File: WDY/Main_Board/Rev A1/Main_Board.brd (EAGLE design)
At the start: 130 x 70 mm, 193 parts, among them J1 22-05-7028-02, J10 22-05-7038-03, J11 22-05-7028-02, J12 22-05-7028-02, J13 22-05-7028-02, J14 22-05-7028-02, J15 22-05-7058-05, J16 22-27-2061-06, J2 22-05-7028-02, J3 22-05-7048-04, J4 22-05-7048-04, J5 1241050-5, J6 90814-0208, J7 90814-0206, J8 90814-0208, J9 22-05-7038-03, K1 G6K-2G-Y, K2 G6K-2G-Y, K3 G6K-2G-Y, K4 G6K-2G-Y, P1 RB1-125BAG1A, SW1 B3FS-1015, SW2 B3FS-1015, T1 MMBT2222AL, U1 LPC1768FBD100, U11 SN74LVC3G17DCTR, U2 SN74LVC3G17DCTR, U3 SN74LVC3G17DCTR, U4 TPL0401A, U5 AT24C512C-SSHM-B, U6 SN74LVC2G17DBVR, U7 SN74LVC2G17DBVR, U8 LT1767EMS8E-5PBF, U9 TC1264-3.3, X1 FC-135, X2 MSTBA2

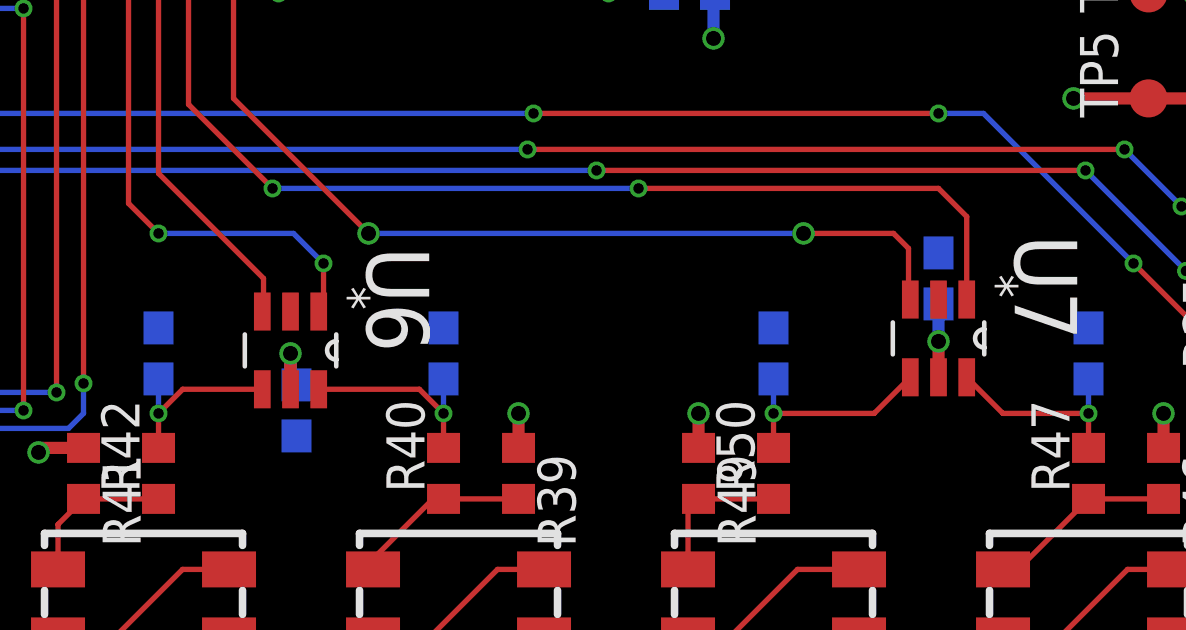
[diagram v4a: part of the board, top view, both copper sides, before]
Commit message: Fix :  Inverted input / output on all SN74LVC (U6 and U7)
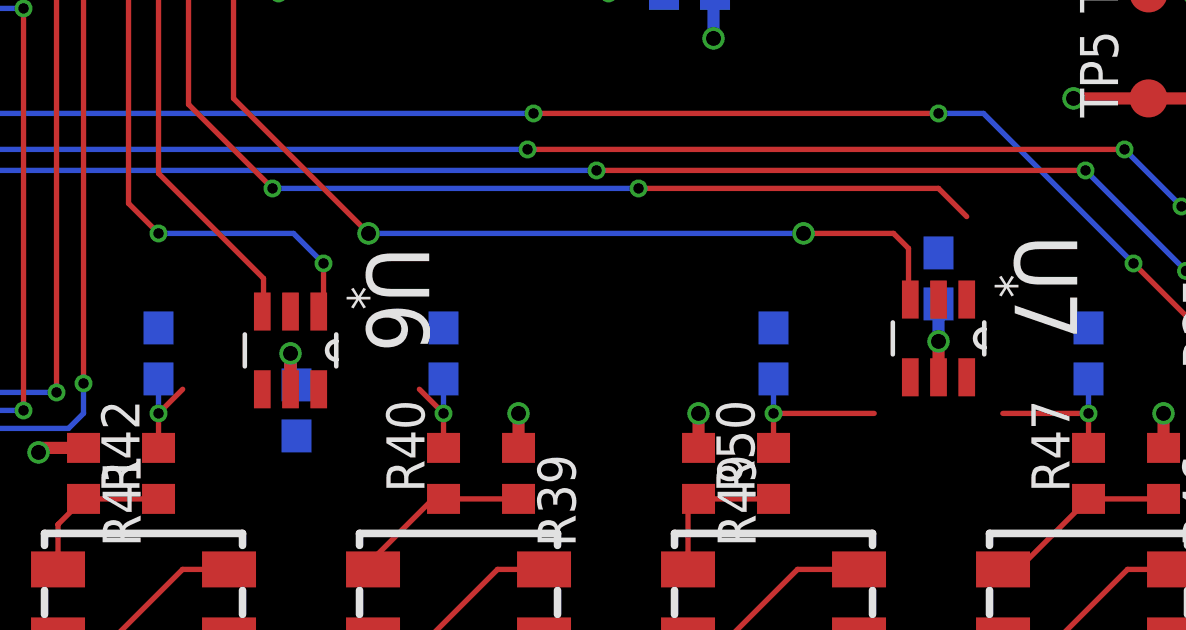
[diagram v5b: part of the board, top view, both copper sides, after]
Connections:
- net BRAKE_SENSOR_1: no longer U6.1
- net BRAKE_SENSOR_2: no longer U6.3
- net DRIVE_EN: now also U7.6; no longer U7.1
- net DRIVE_ERR: now also U7.4; no longer U7.3
- net N$38: no longer U6.4
- net N$39: no longer U6.6
- net N$41: now also U7.1; no longer U7.6
- net N$42: now also U7.3; no longer U7.4
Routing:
- net N$39: track 6.79 -> 3.44 mm
- net DRIVE_EN: track 65.2 -> 62.5 mm
- net N$38: track 6.09 -> 3.44 mm
- net N$42: track 7.36 -> 5.66 mm
- net N$41: track 6.86 -> 5.16 mm
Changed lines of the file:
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@@
 <contactref element="R42" pad="2"/>
 <contactref element="C25" pad="1"/>
-<contactref element="U6" pad="4"/>
 <wire x1="84.5" y1="22.15" x2="84.5" y2="21" width="0.1778" layer="16"/>
 <via x="84.5" y="21" extent="1-16" drill="0.35"/>
 <wire x1="84.5" y1="21" x2="84.5" y2="19.85" width="0.1778" layer="1"/>
-<wire x1="87.9602" y1="21.8046" x2="85.3046" y2="21.8046" width="0.1778" layer="1"/>
 <wire x1="85.3046" y1="21.8046" x2="84.5" y2="21" width="0.1778" layer="1"/>
 </signal>
 <signal name="N$39">
-<contactref element="U6" pad="6"/>
 <contactref element="R40" pad="2"/>
 <contactref element="C26" pad="1"/>
@@
 <via x="94" y="21" extent="1-16" drill="0.35"/>
 <wire x1="94" y1="21" x2="94" y2="19.85" width="0.1778" layer="1"/>
-<wire x1="89.8398" y1="21.8046" x2="93.1954" y2="21.8046" width="0.1778" layer="1"/>
 <wire x1="93.1954" y1="21.8046" x2="94" y2="21" width="0.1778" layer="1"/>
 </signal>
 <signal name="BRAKE_SENSOR_1">
-<contactref element="U6" pad="1"/>
 <contactref element="U1" pad="81"/>
-<wire x1="89.8398" y1="24.3954" x2="90" y2="24.5556" width="0.1778" layer="1"/>
 <wire x1="90" y1="24.5556" x2="90" y2="26" width="0.1778" layer="1"/>
 <wire x1="59.88" y1="40" x2="65" y2="40" width="0.1778" layer="1"/>
@@
 </signal>
 <signal name="BRAKE_SENSOR_2">
-<contactref element="U6" pad="3"/>
 <contactref element="U1" pad="80"/>
-<wire x1="87.9602" y1="24.3954" x2="88" y2="24.4352" width="0.1778" layer="1"/>
 <wire x1="88" y1="24.4352" x2="88" y2="25.5" width="0.1778" layer="1"/>
 <wire x1="64" y1="40.7" x2="63.8" y2="40.5" width="0.1778" layer="1"/>
@@
 </signal>
 <signal name="N$41">
-<contactref element="U7" pad="6"/>
 <contactref element="C28" pad="1"/>
 <contactref element="R47" pad="2"/>
@@
 <via x="115.5" y="21" extent="1-16" drill="0.35"/>
 <wire x1="115.5" y1="21" x2="115.5" y2="19.85" width="0.1778" layer="1"/>
-<wire x1="111.4398" y1="22.2046" x2="112.6444" y2="21" width="0.1778" layer="1"/>
 <wire x1="112.6444" y1="21" x2="115.5" y2="21" width="0.1778" layer="1"/>
+<contactref element="U7" pad="1"/>
+<wire x1="111.4398" y1="24.7954" x2="112.6444" y2="21" width="0" layer="19" extent="1-1"/>
 </signal>
 <signal name="N$42">
-<contactref element="U7" pad="4"/>
 <contactref element="C27" pad="1"/>
 <contactref element="R50" pad="2"/>
@@
 <via x="105" y="21" extent="1-16" drill="0.35"/>
 <wire x1="105" y1="21" x2="105" y2="19.85" width="0.1778" layer="1"/>
-<wire x1="109.5602" y1="22.2046" x2="108.3556" y2="21" width="0.1778" layer="1"/>
 <wire x1="108.3556" y1="21" x2="105" y2="21" width="0.1778" layer="1"/>
+<contactref element="U7" pad="3"/>
+<wire x1="108.3556" y1="21" x2="109.5602" y2="24.7954" width="0" layer="19" extent="1-1"/>
 </signal>
 <signal name="DRIVE_EN">
-<contactref element="U7" pad="1"/>
 <contactref element="U1" pad="79"/>
 <wire x1="110.5" y1="28.5" x2="100.5" y2="28.5" width="0.1778" layer="1"/>
@@
 <wire x1="85.5" y1="31.3" x2="88.3" y2="28.5" width="0.1778" layer="1"/>
 <via x="84.2" y="41.3" extent="1-16" drill="0.35"/>
-<wire x1="111.4398" y1="24.7954" x2="111.4398" y2="27.5602" width="0.1778" layer="1"/>
 <wire x1="111.4398" y1="27.5602" x2="110.5" y2="28.5" width="0.1778" layer="1"/>
+<contactref element="U7" pad="6"/>
+<wire x1="111.4398" y1="27.5602" x2="111.4398" y2="22.2046" width="0" layer="19" extent="1-1"/>
 </signal>
 <signal name="DRIVE_ERR">
-<contactref element="U7" pad="3"/>
 <contactref element="U1" pad="78"/>
 <wire x1="106" y1="27" x2="91.5" y2="27" width="0.1778" layer="16"/>
@@
 <via x="91.5" y="27" extent="1-16" drill="0.5"/>
 <via x="85.6" y="41.9" extent="1-16" drill="0.35"/>
-<wire x1="109.5602" y1="24.7954" x2="109.5" y2="24.8556" width="0.1778" layer="1"/>
 <wire x1="109.5" y1="24.8556" x2="109.5" y2="26.5" width="0.1778" layer="1"/>
 <wire x1="109.5" y1="26.5" x2="109" y2="27" width="0.1778" layer="1"/>
 <wire x1="109" y1="27" x2="106" y2="27" width="0.1778" layer="1"/>
+<contactref element="U7" pad="4"/>
+<wire x1="109.5" y1="24.8556" x2="109.5602" y2="22.2046" width="0" layer="19" extent="1-1"/>
 </signal>
 <signal name="RTCX1">

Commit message: Rotate U$15
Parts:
- moved C53 4.30 mm to (88.9, 25.4), turned to 90 degrees
- moved U$14 1.50 mm to (6.00, 53.4), flipped to the top, turned to 90 degrees
- moved JP1 1.40 mm to (1.00, 39.6)
- moved C52 0.30 mm to (110.5, 25.2)
- turned U6 to 90 degrees
- turned U7 to 90 degrees
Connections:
- net BRAKE_SENSOR_1: now also U6.6
- net BRAKE_SENSOR_2: now also U6.4
- net N$38: now also U6.3
- net N$39: now also U6.1
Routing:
- net VBAT+: track 4.83 -> 99.7 mm, vias 1 -> 2
- net AVDD: track 16.7 -> 7.73 mm
- net N$39: track 3.44 -> 11.2 mm, vias 1 -> 3
- net N$38: track 3.44 -> 9.31 mm, vias 1 -> 3
- net N$41: track 5.16 -> 10.1 mm, vias 1 -> 3
- net N$42: track 5.66 -> 10.5 mm, vias 1 -> 3
- net BRAKE_SENSOR_1: track 43.8 -> 41.1 mm, vias 4 -> 2
- net BRAKE_SENSOR_2: track 42.1 -> 44.4 mm
- net DRIVE_ERR: track 63.1 -> 65.3 mm
- net N$22: track 34.0 -> 32.6 mm
- net DRIVE_EN: track 62.5 -> 63.0 mm
- net +3V3: track 156.1 -> 156.6 mm
- removed copper zone on layer 3, net VBAT+

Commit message: Put boot and reset button on top layer
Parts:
- moved SW1 1.12 mm to (107.2, 39.0), flipped to the top, turned to 0 degrees
- moved SW2 1.12 mm to (94.5, 39.0), flipped to the top, turned to 180 degrees
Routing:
- net RESET: track 62.7 -> 69.0 mm
- net N$5: track 14.7 -> 19.6 mm, vias 0 -> 1
- net +3V3: track 156.6 -> 152.8 mm
- net JTAG_TCK: track 32.7 -> 30.2 mm
- net JTAG_TMS: track 32.6 -> 30.1 mm
- net JTAG_TDI: track 35.1 -> 33.0 mm
- net JTAG_TDO: track 37.2 -> 35.2 mm
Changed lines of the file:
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@@
 <grid distance="0.5" unitdist="mm" unit="mm" style="lines" multiple="1" display="no" altdistance="0.1" altunitdist="mm" altunit="mm"/>
 <layers>
-<layer number="1" name="Top" color="4" fill="1" visible="yes" active="yes"/>
-<layer number="2" name="Route2" color="6" fill="1" visible="yes" active="yes"/>
+<layer number="1" name="Top" color="4" fill="1" visible="no" active="yes"/>
+<layer number="2" name="Route2" color="6" fill="1" visible="no" active="yes"/>
 <layer number="3" name="Route3" color="20" fill="1" visible="no" active="yes"/>
 <layer number="14" name="Route14" color="1" fill="6" visible="no" active="no"/>
@@
 <layer number="19" name="Unrouted" color="6" fill="1" visible="yes" active="yes"/>
 <layer number="20" name="Dimension" color="15" fill="1" visible="yes" active="yes"/>
-<layer number="21" name="tPlace" color="7" fill="1" visible="yes" active="yes"/>
+<layer number="21" name="tPlace" color="7" fill="1" visible="no" active="yes"/>
 <layer number="22" name="bPlace" color="7" fill="1" visible="yes" active="yes"/>
-<layer number="23" name="tOrigins" color="15" fill="1" visible="yes" active="yes"/>
+<layer number="23" name="tOrigins" color="15" fill="1" visible="no" active="yes"/>
 <layer number="24" name="bOrigins" color="15" fill="1" visible="yes" active="yes"/>
-<layer number="25" name="tNames" color="7" fill="1" visible="yes" active="yes"/>
+<layer number="25" name="tNames" color="7" fill="1" visible="no" active="yes"/>
 <layer number="26" name="bNames" color="7" fill="1" visible="yes" active="yes"/>
-<layer number="27" name="tValues" color="7" fill="1" visible="yes" active="yes"/>
+<layer number="27" name="tValues" color="7" fill="1" visible="no" active="yes"/>
 <layer number="28" name="bValues" color="7" fill="1" visible="yes" active="yes"/>
 <layer number="29" name="tStop" color="7" fill="3" visible="no" active="yes"/>
@@
 <layer number="49" name="Reference" color="7" fill="1" visible="yes" active="yes"/>
 <layer number="50" name="dxf" color="7" fill="1" visible="yes" active="yes"/>
-<layer number="51" name="tDocu" color="7" fill="1" visible="yes" active="yes"/>
+<layer number="51" name="tDocu" color="7" fill="1" visible="no" active="yes"/>
 <layer number="52" name="bDocu" color="7" fill="1" visible="yes" active="yes"/>
 <layer number="53" name="tGND_GNDA" color="7" fill="1" visible="yes" active="yes"/>
@@
 </element>
 <element name="C55" library="rcl" package="C0603" value="0.1uF" x="74.5" y="22.3"/>
-<element name="SW1" library="Switch_SMT" package="B3FS" value="B3FS-1015" x="106.2" y="39.5" rot="MR180"/>
-<element name="SW2" library="Switch_SMT" package="B3FS" value="B3FS-1015" x="93.5" y="39.5" rot="MR0"/>
+<element name="SW1" library="Switch_SMT" package="B3FS" value="B3FS-1015" x="107.2" y="39"/>
+<element name="SW2" library="Switch_SMT" package="B3FS" value="B3FS-1015" x="94.5" y="39" rot="R180"/>
 <element name="R11" library="rcl" package="R0603" value="10K" x="102.2" y="35" rot="MR180"/>
 <element name="R67" library="rcl" package="R0603" value="10K" x="90.9" y="43.9" rot="MR180"/>
@@
 <wire x1="66.5" y1="24.36" x2="66.5" y2="23.3" width="0.4064" layer="16"/>
 <wire x1="66.5" y1="23.3" x2="66.2" y2="23" width="0.4064" layer="16"/>
-<wire x1="29" y1="32.58" x2="29" y2="36.4" width="0.4064" layer="16"/>
 <wire x1="35.5" y1="33.8" x2="34.1" y2="33.8" width="0.4064" layer="1"/>
 <wire x1="34.1" y1="33.8" x2="33.5" y2="34.4" width="0.4064" layer="1"/>
@@
 <wire x1="73.7" y1="24.425" x2="75.3" y2="24.425" width="0.4064" layer="1"/>
 <wire x1="75.3" y1="24.425" x2="75.325" y2="24.45" width="0.4064" layer="1"/>
+<wire x1="29" y1="35.35" x2="29" y2="32.58" width="0" layer="19" extent="1-16"/>
 </signal>
 <signal name="N$4">
@@
 <contactref element="U1" pad="1"/>
 <contactref element="J5" pad="9"/>
-<wire x1="29" y1="22.42" x2="30.92" y2="22.42" width="0.1778" layer="16"/>
 <wire x1="30.92" y1="22.42" x2="31.5" y2="23" width="0.1778" layer="16"/>
 <wire x1="31.5" y1="23" x2="31.5" y2="25.5" width="0.1778" layer="16"/>
 <wire x1="31.5" y1="25.5" x2="32" y2="26" width="0.1778" layer="16"/>
-<wire x1="32" y1="26" x2="45" y2="26" width="0.1778" layer="16"/>
-<wire x1="45" y1="26" x2="45.9" y2="26" width="0.1778" layer="16"/>
+<wire x1="32" y1="26" x2="45.9" y2="26" width="0.1778" layer="16"/>
 <wire x1="45.9" y1="26" x2="46" y2="26.1" width="0.1778" layer="16"/>
 <via x="46" y="26.1" extent="1-16" drill="0.35"/>
@@
 <wire x1="61.5" y1="28" x2="61.5" y2="28.88" width="0.1778" layer="1"/>
 <wire x1="46" y1="26.1" x2="47.4" y2="27.5" width="0.1778" layer="1"/>
+<wire x1="29" y1="22.42" x2="30.92" y2="22.42" width="0" layer="19" extent="16-16"/>
 </signal>
 <signal name="JTAG_TDI" class="1">
@@
 <contactref element="J5" pad="7"/>
 <wire x1="29" y1="24.96" x2="29.96" y2="24.96" width="0.1778" layer="16"/>
-<wire x1="29.96" y1="24.96" x2="31.5" y2="26.5" width="0.1778" layer="16"/>
 <wire x1="62" y1="28.88" x2="62" y2="28" width="0.1778" layer="1"/>
 <wire x1="62" y1="28" x2="61" y2="27" width="0.1778" layer="1"/>
@@
 <wire x1="36.7" y1="26.7" x2="36.5" y2="26.5" width="0.1778" layer="16"/>
 <wire x1="36.5" y1="26.5" x2="31.5" y2="26.5" width="0.1778" layer="16"/>
+<wire x1="29.96" y1="24.96" x2="31.5" y2="26.5" width="0" layer="19" extent="16-16"/>
 </signal>
 <signal name="JTAG_TMS" class="1">
@@
 <contactref element="J5" pad="10"/>
 <wire x1="34" y1="22.42" x2="34.08" y2="22.5" width="0.1778" layer="16"/>
-<wire x1="34.08" y1="22.5" x2="36.5" y2="22.5" width="0.1778" layer="16"/>
 <wire x1="36.5" y1="22.5" x2="38.9" y2="24.9" width="0.1778" layer="16"/>
 <wire x1="38.9" y1="24.9" x2="49" y2="24.9" width="0.1778" layer="16"/>
@@
 <wire x1="61.5" y1="26.5" x2="62.5" y2="27.5" width="0.1778" layer="1"/>
 <wire x1="62.5" y1="27.5" x2="62.5" y2="28.88" width="0.1778" layer="1"/>
+<wire x1="34.08" y1="22.5" x2="36.5" y2="22.5" width="0" layer="19" extent="16-16"/>
 </signal>
 <signal name="JTAG_TCK" class="1">
@@
 <contactref element="J5" pad="8"/>
 <wire x1="34" y1="24.96" x2="34.04" y2="25" width="0.1778" layer="16"/>
-<wire x1="34.04" y1="25" x2="36.5" y2="25" width="0.1778" layer="16"/>
 <wire x1="36.5" y1="25" x2="37" y2="25.5" width="0.1778" layer="16"/>
 <wire x1="37" y1="25.5" x2="47.5" y2="25.5" width="0.1778" layer="16"/>
@@
 <wire x1="63.5" y1="26.5" x2="63.5" y2="28.88" width="0.1778" layer="1"/>
 <wire x1="63.5" y1="26.5" x2="62.3" y2="25.3" width="0.1778" layer="1"/>
+<wire x1="34.04" y1="25" x2="36.5" y2="25" width="0" layer="19" extent="16-16"/>
 </signal>
 <signal name="JTAG_RST" class="1">
@@
 <via x="72.8" y="37.6" extent="1-16" drill="0.35"/>
 <via x="72.8" y="34.8" extent="1-16" drill="0.35"/>
-<wire x1="102.2" y1="37.25" x2="110.2" y2="37.25" width="0.1778" layer="16"/>
+<wire x1="103.2" y1="41.25" x2="111.2" y2="41.25" width="0.1778" layer="1"/>
 <wire x1="101.35" y1="35" x2="99.5" y2="35" width="0.1778" layer="16"/>
 <wire x1="72.8" y1="37.6" x2="85.9" y2="37.6" width="0.1778" layer="16"/>
@@
 <wire x1="88.5" y1="35" x2="99.5" y2="35" width="0.1778" layer="1"/>
 <via x="99.5" y="35" extent="1-16" drill="0.35"/>
-<wire x1="101.35" y1="35" x2="101.35" y2="35.85" width="0.1778" layer="16"/>
-<wire x1="101.35" y1="35.85" x2="102.2" y2="36.7" width="0.1778" layer="16"/>
-<wire x1="102.2" y1="36.7" x2="102.2" y2="37.25" width="0.1778" layer="16"/>
+<wire x1="103.2" y1="41.8" x2="103.2" y2="41.25" width="0.1778" layer="1"/>
+<wire x1="103.2" y1="41.25" x2="102.25" y2="41.25" width="0.1778" layer="1"/>
+<wire x1="102.25" y1="41.25" x2="101.5" y2="40.5" width="0.1778" layer="1"/>
+<wire x1="101.5" y1="40.5" x2="101.5" y2="37" width="0.1778" layer="1"/>
+<wire x1="101.5" y1="37" x2="99.5" y2="35" width="0.1778" layer="1"/>
 </signal>
 <signal name="HMI_LCD_BACKLIGHT">
@@
 <contactref element="SW2" pad="4"/>
 <contactref element="SW2" pad="3"/>
-<wire x1="89.5" y1="41.75" x2="97.5" y2="41.75" width="0.1778" layer="16"/>
+<wire x1="90.5" y1="36.75" x2="98.5" y2="36.75" width="0.1778" layer="1"/>
 <contactref element="R71" pad="2"/>
 <contactref element="R72" pad="2"/>
@@
 <wire x1="89.85" y1="46" x2="89.85" y2="44.1" width="0.1778" layer="16"/>
 <wire x1="89.85" y1="44.1" x2="90.05" y2="43.9" width="0.1778" layer="16"/>
-<wire x1="90.05" y1="43.9" x2="90.05" y2="42.3" width="0.1778" layer="16"/>
-<wire x1="90.05" y1="42.3" x2="89.5" y2="41.75" width="0.1778" layer="16"/>
+<wire x1="90.5" y1="36.75" x2="90.5" y2="39" width="0.1778" layer="1"/>
+<via x="90.5" y="39" extent="1-16" drill="0.35"/>
+<wire x1="90.5" y1="39" x2="90.05" y2="39.45" width="0.1778" layer="16"/>
+<wire x1="90.05" y1="39.45" x2="90.05" y2="43.9" width="0.1778" layer="16"/>
 </signal>
 <signal name="BOOT_SELECT_P2_12" class="1">
@@
 <via x="76" y="46" extent="1-16" drill="0.35"/>
 <wire x1="76" y1="46" x2="84.5" y2="46" width="0.1778" layer="16"/>
-<wire x1="86.6" y1="48.1" x2="88.15" y2="48.1" width="0.1778" layer="16"/>
 <wire x1="86.6" y1="48.1" x2="84.5" y2="46" width="0.1778" layer="16"/>
+<wire x1="86.6" y1="48.1" x2="88.15" y2="48.1" width="0.1778" layer="16"/>
 </signal>
 </signals>

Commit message: Put J16 on top layer
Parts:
- flipped J16 to the top
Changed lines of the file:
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@@
 <grid distance="0.5" unitdist="mm" unit="mm" style="lines" multiple="1" display="no" altdistance="0.1" altunitdist="mm" altunit="mm"/>
 <layers>
-<layer number="1" name="Top" color="4" fill="1" visible="no" active="yes"/>
-<layer number="2" name="Route2" color="6" fill="1" visible="no" active="yes"/>
+<layer number="1" name="Top" color="4" fill="1" visible="yes" active="yes"/>
+<layer number="2" name="Route2" color="6" fill="1" visible="yes" active="yes"/>
 <layer number="3" name="Route3" color="20" fill="1" visible="no" active="yes"/>
 <layer number="14" name="Route14" color="1" fill="6" visible="no" active="no"/>
@@
 <layer number="19" name="Unrouted" color="6" fill="1" visible="yes" active="yes"/>
 <layer number="20" name="Dimension" color="15" fill="1" visible="yes" active="yes"/>
-<layer number="21" name="tPlace" color="7" fill="1" visible="no" active="yes"/>
+<layer number="21" name="tPlace" color="7" fill="1" visible="yes" active="yes"/>
 <layer number="22" name="bPlace" color="7" fill="1" visible="yes" active="yes"/>
-<layer number="23" name="tOrigins" color="15" fill="1" visible="no" active="yes"/>
+<layer number="23" name="tOrigins" color="15" fill="1" visible="yes" active="yes"/>
 <layer number="24" name="bOrigins" color="15" fill="1" visible="yes" active="yes"/>
-<layer number="25" name="tNames" color="7" fill="1" visible="no" active="yes"/>
+<layer number="25" name="tNames" color="7" fill="1" visible="yes" active="yes"/>
 <layer number="26" name="bNames" color="7" fill="1" visible="yes" active="yes"/>
-<layer number="27" name="tValues" color="7" fill="1" visible="no" active="yes"/>
+<layer number="27" name="tValues" color="7" fill="1" visible="yes" active="yes"/>
 <layer number="28" name="bValues" color="7" fill="1" visible="yes" active="yes"/>
 <layer number="29" name="tStop" color="7" fill="3" visible="no" active="yes"/>
@@
 <layer number="49" name="Reference" color="7" fill="1" visible="yes" active="yes"/>
 <layer number="50" name="dxf" color="7" fill="1" visible="yes" active="yes"/>
-<layer number="51" name="tDocu" color="7" fill="1" visible="no" active="yes"/>
+<layer number="51" name="tDocu" color="7" fill="1" visible="yes" active="yes"/>
 <layer number="52" name="bDocu" color="7" fill="1" visible="yes" active="yes"/>
 <layer number="53" name="tGND_GNDA" color="7" fill="1" visible="yes" active="yes"/>
@@
 <element name="U$14" library="keystone" package="3000" value="3000" x="6" y="53.4" rot="R90"/>
 <element name="R70" library="rcl" package="R0603" value="100" x="74.9" y="50.4" rot="R270"/>
-<element name="J16" library="con-molex" package="6410-06" value="22-27-2061-06" x="37" y="59.5" rot="MR270">
-<attribute name="MF" value="" x="37" y="59.5" size="1.778" layer="28" ratio="10" rot="MR270" display="off"/>
-<attribute name="OC_FARNELL" value="unknown" x="37" y="59.5" size="1.778" layer="28" ratio="10" rot="MR270" display="off"/>
-<attribute name="MPN" value="" x="37" y="59.5" size="1.778" layer="28" ratio="10" rot="MR270" display="off"/>
-<attribute name="OC_NEWARK" value="unknown" x="37" y="59.5" size="1.778" layer="28" ratio="10" rot="MR270" display="off"/>
+<element name="J16" library="con-molex" package="6410-06" value="22-27-2061-06" x="37" y="59.5" rot="R270">
+<attribute name="MF" value="" x="37" y="59.5" size="1.778" layer="27" ratio="10" rot="R270" display="off"/>
+<attribute name="OC_FARNELL" value="unknown" x="37" y="59.5" size="1.778" layer="27" ratio="10" rot="R270" display="off"/>
+<attribute name="MPN" value="" x="37" y="59.5" size="1.778" layer="27" ratio="10" rot="R270" display="off"/>
+<attribute name="OC_NEWARK" value="unknown" x="37" y="59.5" size="1.778" layer="27" ratio="10" rot="R270" display="off"/>
 </element>
 <element name="TP3" library="testpad" package="B1,27" value="TPB1,27" x="128" y="31.5">
@@
 <wire x1="75" y1="45.4" x2="84.9" y2="45.4" width="0.1778" layer="16"/>
 <wire x1="84.9" y1="45.4" x2="85.5" y2="46" width="0.1778" layer="16"/>
-<wire x1="85.5" y1="46" x2="88.15" y2="46" width="0.1778" layer="16"/>
+<wire x1="88.15" y1="46" x2="85.5" y2="46" width="0.1778" layer="16"/>
 </signal>
 <signal name="BOOT_SELECT_P2_10" class="1">
